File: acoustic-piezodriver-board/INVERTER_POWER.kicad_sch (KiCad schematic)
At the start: 58 parts, among them Q501 AO3400A, Q502 AO3400A, U501 NCE6005AS, U502 LM3478MM, U503 NCE6005AS, U504 LM3478MM

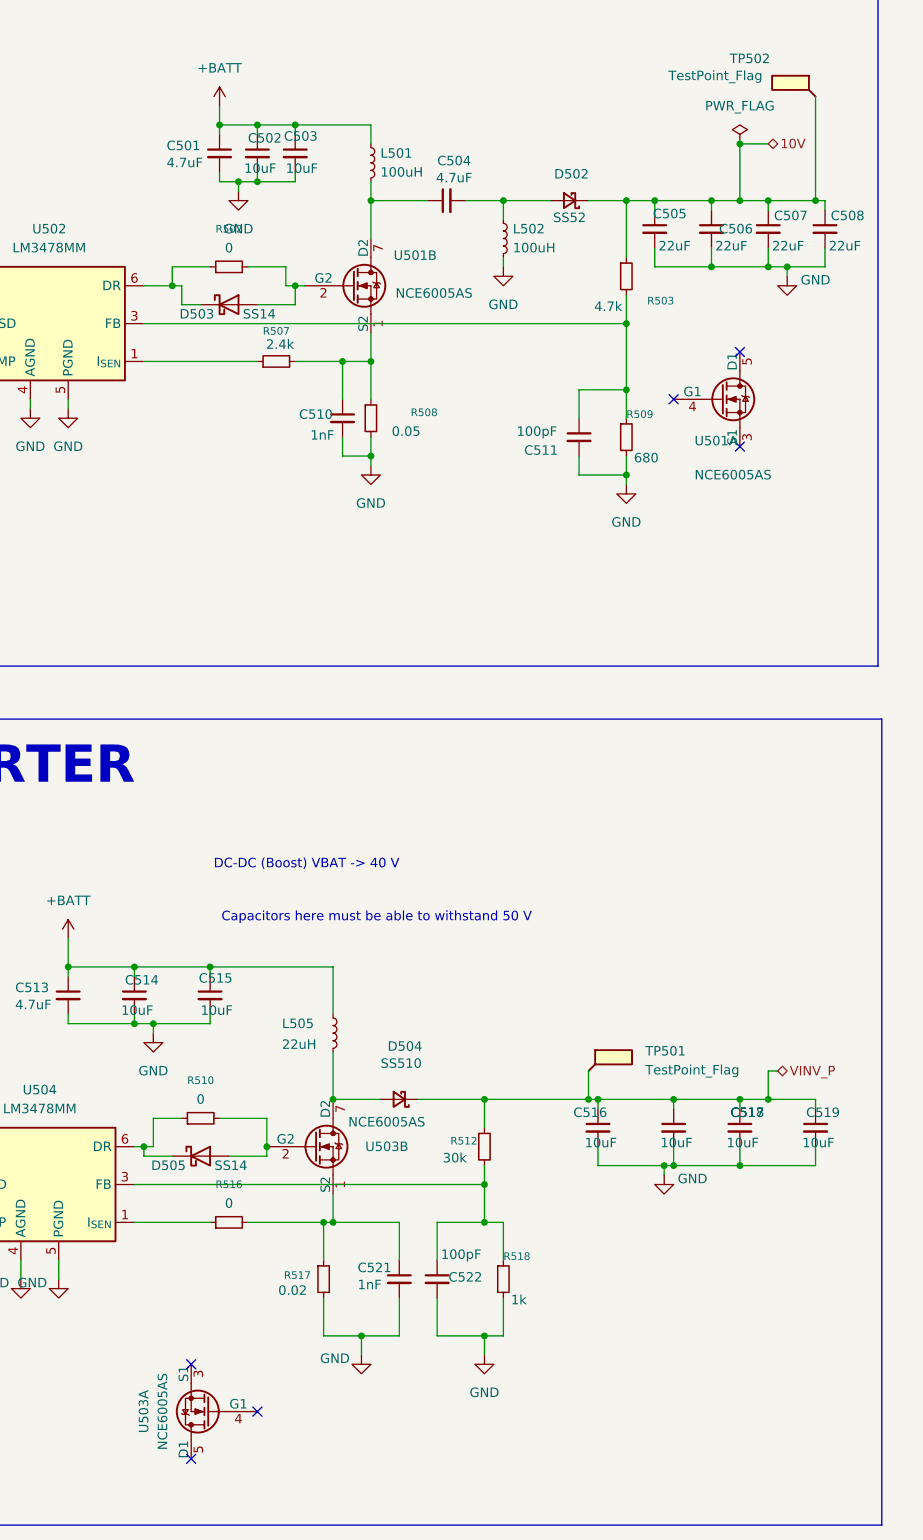
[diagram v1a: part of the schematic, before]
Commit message: changed footprints,  changed stackup from L3:PWR-> L3:GND and routed +BATT on 4th layer
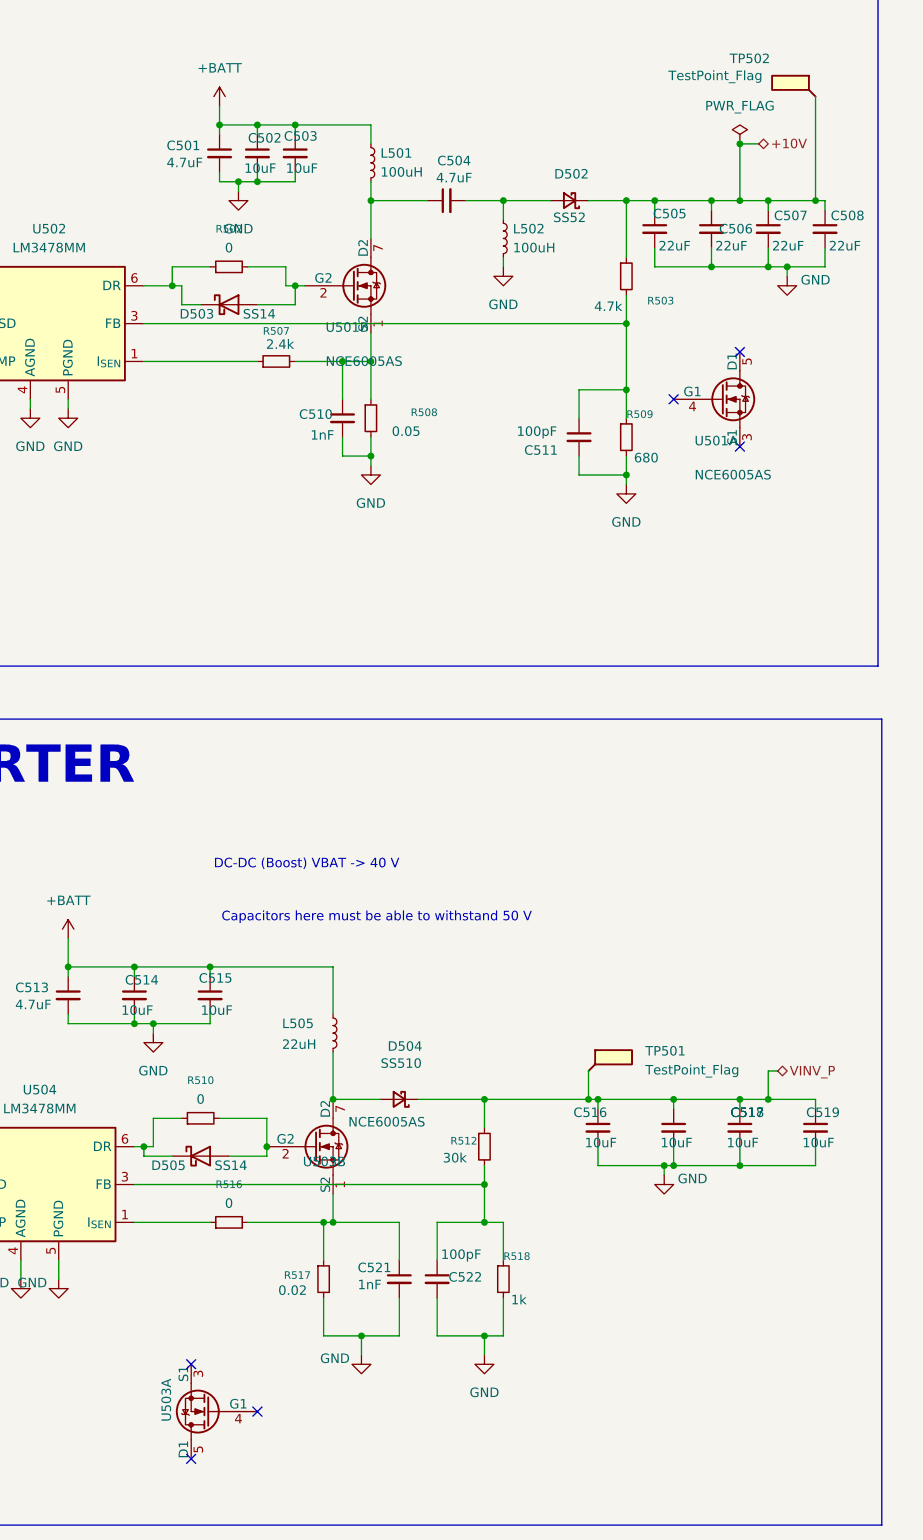
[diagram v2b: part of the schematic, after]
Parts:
- U501, U503: footprint Package_SO:SOP-8-1EP_4.57x4.57mm_P1.27mm_EP4.57x4.45mm_ThermalVias -> Package_SO:SOIC-8_3.9x4.9mm_P1.27mm
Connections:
- net 10V renamed +10V
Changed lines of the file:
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@@
 	)
 	(no_connect
-		(at 309.88 231.14)
-	)
-	(no_connect
 		(at 374.65 101.6)
 	)
@@
 	)
 	(no_connect
+		(at 309.88 231.14)
+	)
+	(no_connect
 		(at 300.99 237.49)
 	)
@@
 	(wire
 		(pts
-			(xy 378.46 60.96) (xy 374.65 60.96)
+			(xy 377.19 60.96) (xy 374.65 60.96)
 		)
 		(stroke
@@
 		)
 	)
-	(hierarchical_label "10V"
+	(hierarchical_label "+10V"
 		(shape bidirectional)
-		(at 378.46 60.96 0)
+		(at 377.19 60.96 0)
 		(effects
 			(font
@@
 			)
 		)
-		(property "Footprint" "Package_SO:SOP-8-1EP_4.57x4.57mm_P1.27mm_EP4.57x4.45mm_ThermalVias"
-			(at 378.46 95.25 0)
+		(property "Footprint" "Package_SO:SOIC-8_3.9x4.9mm_P1.27mm"
+			(at 378.714 99.822 0)
 			(effects
 				(font
@@
 		)
 		(property "Datasheet" "https://jlcpcb.com/api/file/downloadByFileSystemAccessId/8588881119395647488"
-			(at 378.46 95.25 0)
+			(at 378.46 97.79 0)
 			(effects
 				(font
@@
 		)
 		(property "Description" "Dual N-channel Power MOSFET."
-			(at 374.65 95.25 0)
+			(at 377.19 97.282 0)
 			(effects
 				(font
@@
 		)
 		(property "MPN" "NCE6005AS"
-			(at 374.65 95.25 0)
+			(at 374.904 97.028 0)
 			(effects
 				(font
@@
 	)
 	(symbol
+		(lib_name "NCE6005AS_3")
 		(lib_id "custom_mosfet:NCE6005AS")
 		(at 320.04 195.58 0)
@@
 		(dnp no)
 		(property "Reference" "U503"
-			(at 324.358 195.58 0)
+			(at 315.976 197.612 0)
 			(effects
 				(font
@@
 			)
 		)
-		(property "Footprint" "Package_SO:SOP-8-1EP_4.57x4.57mm_P1.27mm_EP4.57x4.45mm_ThermalVias"
+		(property "Footprint" "Package_SO:SOIC-8_3.9x4.9mm_P1.27mm"
 			(at 323.85 195.58 0)
 			(effects
@@
 		(dnp no)
 		(property "Reference" "U501"
-			(at 328.168 75.946 0)
+			(at 319.024 85.598 0)
 			(effects
 				(font
@@
 		)
 		(property "Value" "NCE6005AS"
-			(at 328.422 81.026 0)
+			(at 319.024 90.17 0)
 			(effects
 				(font
@@
 			)
 		)
-		(property "Footprint" "Package_SO:SOP-8-1EP_4.57x4.57mm_P1.27mm_EP4.57x4.45mm_ThermalVias"
-			(at 328.93 80.01 0)
+		(property "Footprint" "Package_SO:SOIC-8_3.9x4.9mm_P1.27mm"
+			(at 329.184 84.582 0)
 			(effects
 				(font
@@
 		)
 		(property "Datasheet" "https://jlcpcb.com/api/file/downloadByFileSystemAccessId/8588881119395647488"
-			(at 328.93 80.01 0)
+			(at 328.93 82.55 0)
 			(effects
 				(font
@@
 		)
 		(property "Description" "Dual N-channel Power MOSFET."
-			(at 325.12 80.01 0)
+			(at 327.66 82.042 0)
 			(effects
 				(font
@@
 		)
 		(property "MPN" "NCE6005AS"
-			(at 325.12 80.01 0)
+			(at 325.374 81.788 0)
 			(effects
 				(font
@@
 		(on_board yes)
 		(dnp no)
-		(fields_autoplaced yes)
 		(property "Reference" "U503"
-			(at 294.64 231.14 90)
+			(at 297.688 229.616 90)
 			(effects
 				(font
@@
 					(size 1.27 1.27)
 				)
+				(hide yes)
 			)
 		)
-		(property "Footprint" "Package_SO:SOP-8-1EP_4.57x4.57mm_P1.27mm_EP4.57x4.45mm_ThermalVias"
+		(property "Footprint" "Package_SO:SOIC-8_3.9x4.9mm_P1.27mm"
 			(at 297.18 231.14 0)
 			(effects

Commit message: [production checks] checked caps, [todo] Think about replacing 220 nF filtering caps in DC-DC to 0402 package (next) check rest of footprints
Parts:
- C509: footprint Capacitor_SMD:C_0603_1608Metric -> Capacitor_SMD:C_0805_2012Metric; LPN (none) -> C5378; MPN (none) -> CL21B224KBFNNNE
- Q501, Q502: LPN (none) -> C20917; MPN (none) -> AO3400A
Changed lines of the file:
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@@
 			)
 		)
+		(property "LPN" "C20917"
+			(at 228.6 96.52 0)
+			(effects
+				(font
+					(size 1.27 1.27)
+				)
+				(hide yes)
+			)
+		)
+		(property "MPN" "AO3400A"
+			(at 228.6 96.52 0)
+			(effects
+				(font
+					(size 1.27 1.27)
+				)
+				(hide yes)
+			)
+		)
 		(pin "3"
 		)
@@
 			)
 		)
-		(property "Footprint" "Capacitor_SMD:C_0603_1608Metric"
+		(property "Footprint" "Capacitor_SMD:C_0805_2012Metric"
 			(at 246.38 95.25 0)
 			(effects
@@
 			)
 		)
+		(property "LPN" "C5378"
+			(at 246.38 95.25 90)
+			(effects
+				(font
+					(size 1.27 1.27)
+				)
+				(hide yes)
+			)
+		)
+		(property "MPN" "CL21B224KBFNNNE"
+			(at 246.38 95.25 90)
+			(effects
+				(font
+					(size 1.27 1.27)
+				)
+				(hide yes)
+			)
+		)
 		(pin "2"
 		)
@@
 			(at 236.22 218.44 0)
 			(effects
+				(font
+					(size 1.27 1.27)
+				)
+				(hide yes)
+			)
+		)
+		(property "LPN" "C20917"
+			(at 236.22 218.44 0)
+			(effects
+				(font
+					(size 1.27 1.27)
+				)
+				(hide yes)
+			)
+		)
+		(property "MPN" "AO3400A"
+			(at 236.22 218.44 0)
+			(effects

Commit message: changed ss520 footprints
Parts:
- D501, D504: footprint Diode_SMD:D_SMA -> Diode_SMD:D_SMC
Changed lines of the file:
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@@
 			)
 		)
-		(property "Description" "Vf 0.55, If 5A"
+		(property "Description" "Vf 0.55, If 5A, DCblock 20 V"
 			(at 351.79 68.58 0)
 			(effects
@@
 			)
 		)
-		(property "Footprint" "Diode_SMD:D_SMA"
+		(property "Footprint" "Diode_SMD:D_SMC"
 			(at 54.61 179.07 90)
 			(effects
@@
 			)
 		)
-		(property "Footprint" "Diode_SMD:D_SMA"
+		(property "Footprint" "Diode_SMD:D_SMC"
 			(at 328.93 189.23 90)
 			(effects

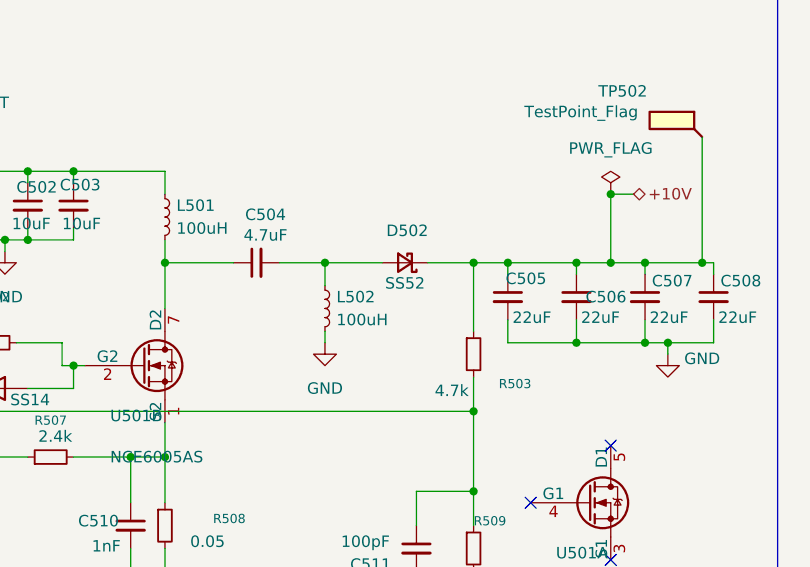
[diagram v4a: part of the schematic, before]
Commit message: checked components until mosfets
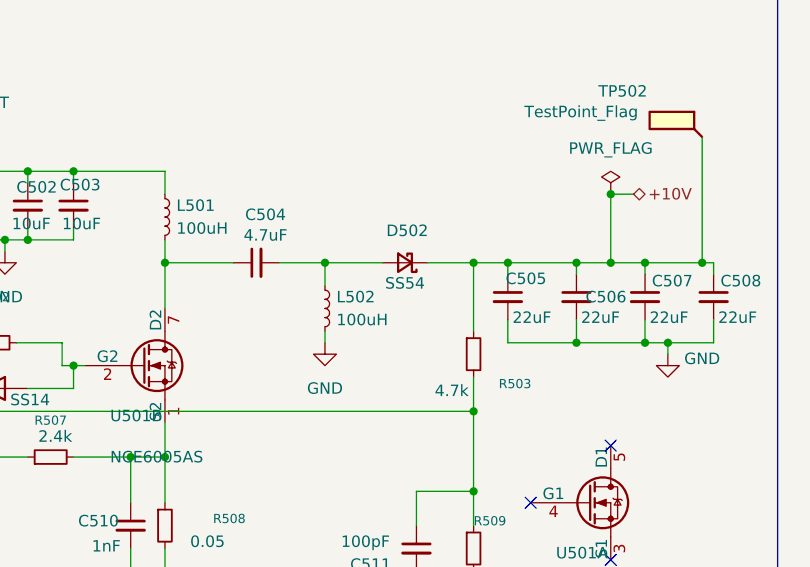
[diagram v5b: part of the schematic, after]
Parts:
- D501, D504: footprint Diode_SMD:D_SMC -> Diode_SMD:D_SMA
- D502: value SS52 -> SS54; footprint Diode_SMD:D_SMA-SMB_Universal_Handsoldering -> Diode_SMD:D_SMA
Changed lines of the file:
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@@
 			)
 		)
-		(property "Value" "SS52"
+		(property "Value" "SS54"
 			(at 351.79 70.866 0)
 			(effects
@@
 			)
 		)
-		(property "Footprint" "Diode_SMD:D_SMA-SMB_Universal_Handsoldering"
+		(property "Footprint" "Diode_SMD:D_SMA"
 			(at 351.79 68.58 90)
 			(effects
@@
 			)
 		)
-		(property "Footprint" "Diode_SMD:D_SMC"
+		(property "Footprint" "Diode_SMD:D_SMA"
 			(at 54.61 179.07 90)
 			(effects
@@
 			)
 		)
-		(property "Footprint" "Diode_SMD:D_SMC"
+		(property "Footprint" "Diode_SMD:D_SMA"
 			(at 328.93 189.23 90)
 			(effects

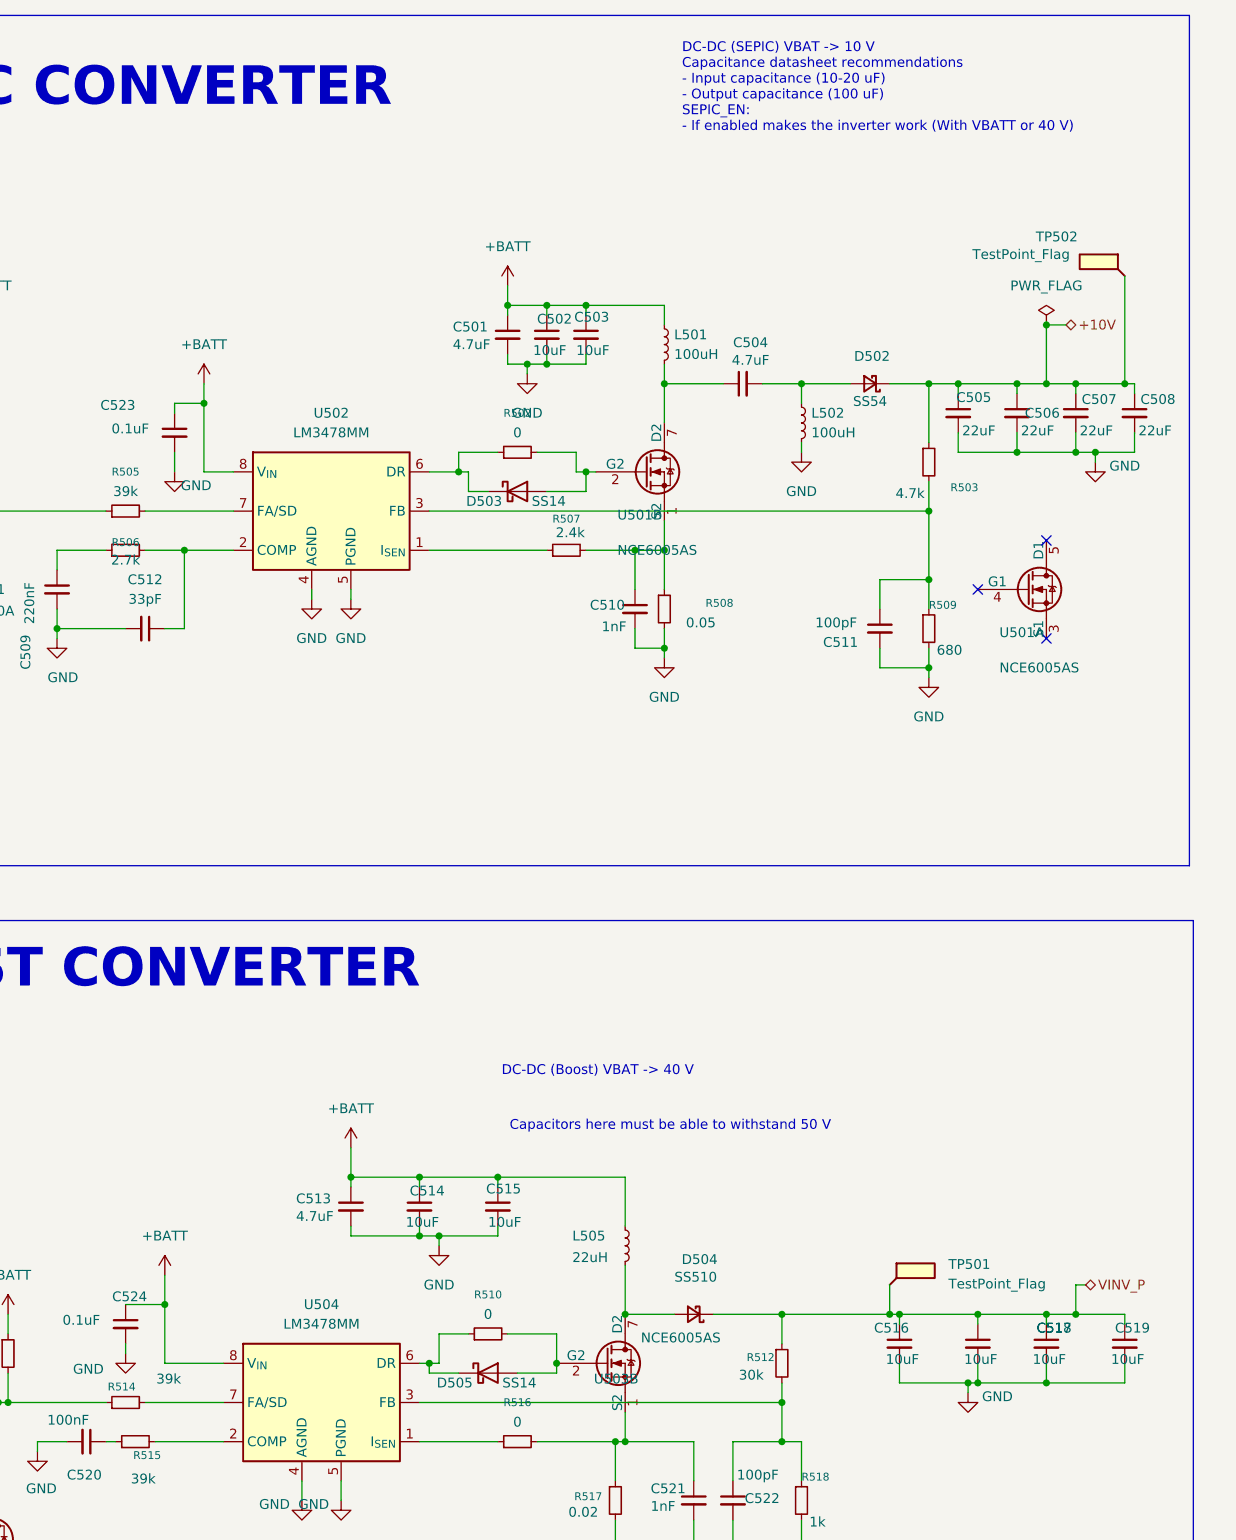
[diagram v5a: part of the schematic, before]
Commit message: completed footprint check (next) reroute pbootstrap circuit on top layer only, fix errors after footprint change
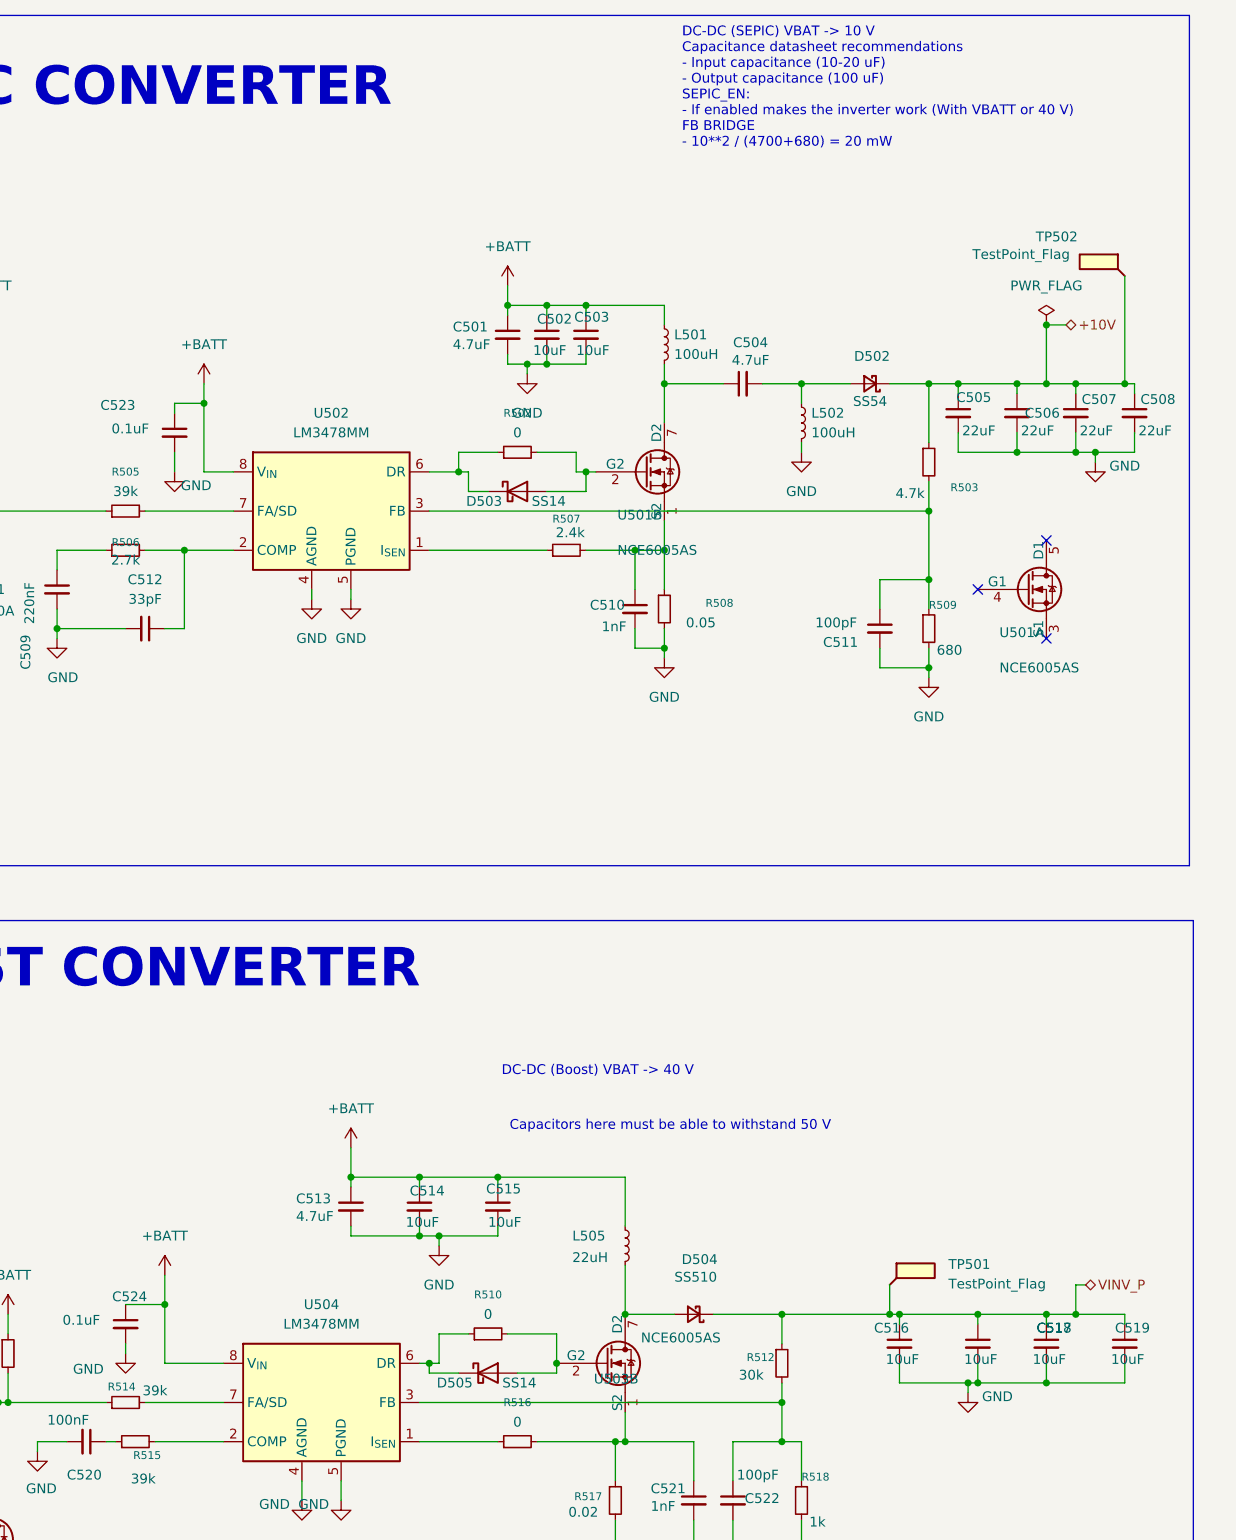
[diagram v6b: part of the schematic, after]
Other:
- note added: "DC-DC (SEPIC) VBAT -> 10 V Capacitance datasheet recommendations - Input capacitance (10-20 uF) - Output capacitance (100 uF) SEPIC_EN: - If enabled makes the inverter work (With VBATT or 40 V) FB BRIDGE - 10**2 / (4700+680) = 20 mW"
- note removed: "DC-DC (SEPIC) VBAT -> 10 V Capacitance datasheet recommendations - Input capacitance (10-20 uF) - Output capacitance (100 uF) SEPIC_EN: - If enabled makes the inverter work (With VBATT or 40 V)"
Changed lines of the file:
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@@
 		)
 	)
-	(text "DC-DC (SEPIC) VBAT -> 10 V\nCapacitance datasheet recommendations\n- Input capacitance (10-20 uF)\n- Output capacitance (100 uF) \nSEPIC_EN:\n- If enabled makes the inverter work (With VBATT or 40 V)"
+	(text "DC-DC (SEPIC) VBAT -> 10 V\nCapacitance datasheet recommendations\n- Input capacitance (10-20 uF)\n- Output capacitance (100 uF) \nSEPIC_EN:\n- If enabled makes the inverter work (With VBATT or 40 V)\nFB BRIDGE\n- 10**2 / (4700+680) = 20 mW"
 		(exclude_from_sim no)
 		(at 327.406 30.226 0)
@@
 		)
 		(property "Value" "39k"
-			(at 260.858 197.612 90)
+			(at 259.08 199.136 90)
 			(effects
 				(font
